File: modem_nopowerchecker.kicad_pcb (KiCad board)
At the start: 2 copper layers, 49.8 x 36.6 mm, 17 parts, among them P1 CONN_01X02, P2 CONN_01X02, P3 CONN_01X04, U1 PC817, U2 7805

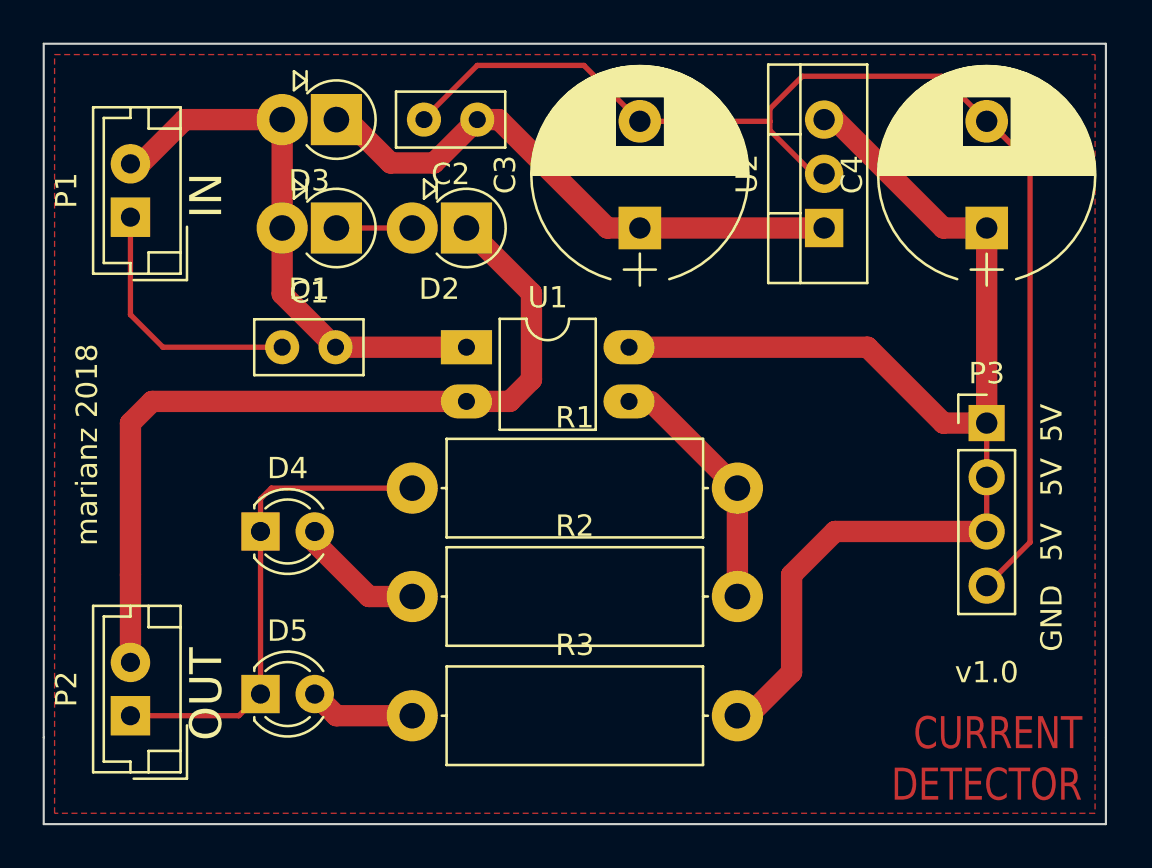
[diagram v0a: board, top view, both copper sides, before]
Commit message: +digital output pin
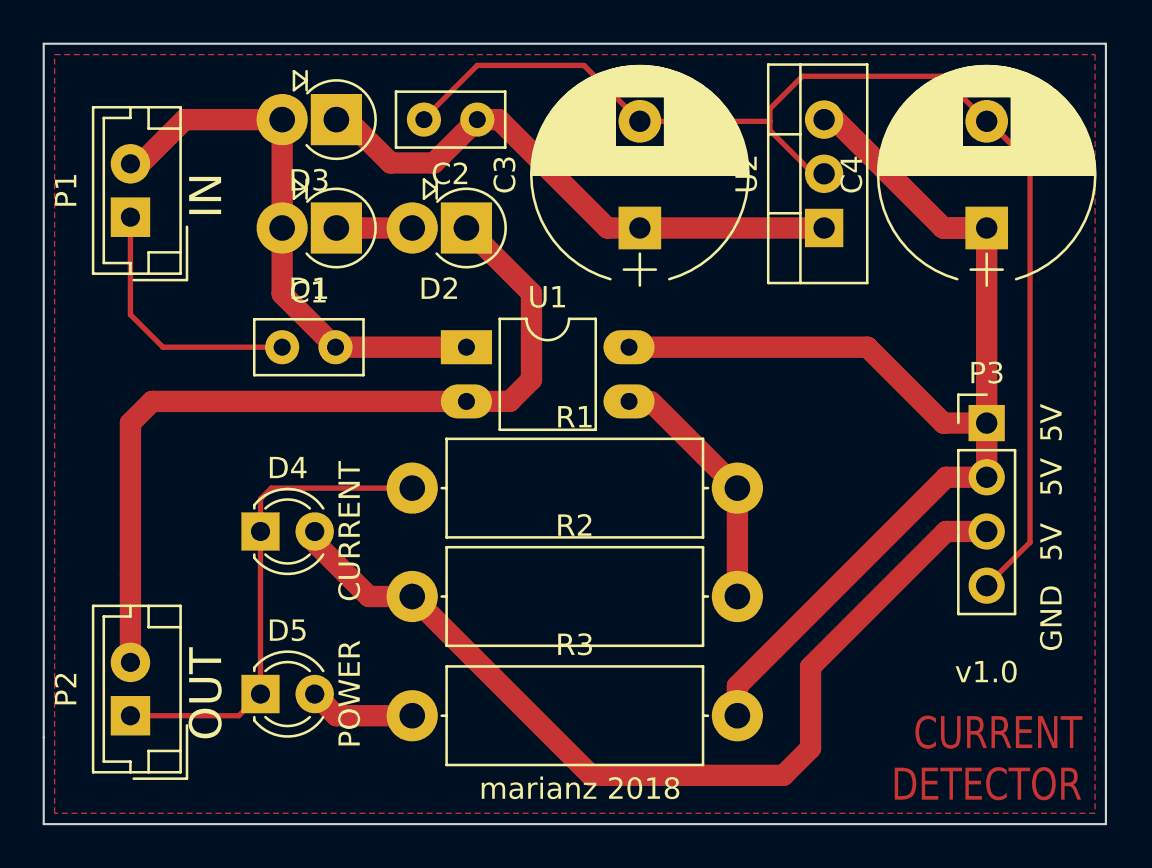
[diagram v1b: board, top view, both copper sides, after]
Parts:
- C1: value C -> 0.1uF
- C2: value C -> 0.1 uF
- C3, C4: value CP -> 100uF/16V
- D1, D2, D3: value D -> 1N4001
- R1, R2: value R -> 1K
- R3: value R -> 10K
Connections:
- P3 pad 3: +5V -> Net-(D4-Pad2)
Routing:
- net Net-(D4-Pad2): track 6.13 -> 43.5 mm
- net +5V: track 61.6 -> 68.0 mm
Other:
- board text added: "CURRENT"
- board text added: "POWER"
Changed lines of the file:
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@@
     (area 87.833999 81.229999 137.718001 117.906001)
     (thickness 1.6)
-    (drawings 15)
-    (tracks 75)
+    (drawings 17)
+    (tracks 81)
     (zones 0)
     (modules 17)
@@
       (outputformat 1)
       (mirror false)
-      (drillshape 1)
+      (drillshape 0)
       (scaleselection 1)
       (outputdirectory ""))
@@
       (effects (font (size 1 1) (thickness 0.15)))
     )
-    (fp_text value C (at 1.25 2.56) (layer F.Fab)
+    (fp_text value 0.1uF (at 1.25 2.56) (layer F.Fab)
       (effects (font (size 1 1) (thickness 0.15)))
     )
@@
       (effects (font (size 1 1) (thickness 0.15)))
     )
-    (fp_text value C (at 1.25 2.56 180) (layer F.Fab)
+    (fp_text value "0.1 uF" (at 1.524 2.286 180) (layer F.Fab)
       (effects (font (size 1 1) (thickness 0.15)))
     )
@@
       (effects (font (size 1 1) (thickness 0.15)))
     )
-    (fp_text value CP (at 2.5 6.31 90) (layer F.Fab)
+    (fp_text value 100uF/16V (at 2.5 6.31 90) (layer F.Fab)
       (effects (font (size 1 1) (thickness 0.15)))
     )
@@
       (effects (font (size 1 1) (thickness 0.15)))
     )
-    (fp_text value CP (at 2.5 6.31 90) (layer F.Fab)
+    (fp_text value 100uF/16V (at 2.5 6.31 90) (layer F.Fab)
       (effects (font (size 1 1) (thickness 0.15)))
     )
@@
       (effects (font (size 1 1) (thickness 0.15)))
     )
-    (fp_text value D (at 1.27 3.749 180) (layer F.Fab)
+    (fp_text value 1N4001 (at 1.27 3.749 180) (layer F.Fab)
       (effects (font (size 1 1) (thickness 0.15)))
     )
@@
       (effects (font (size 1 1) (thickness 0.15)))
     )
-    (fp_text value D (at 1.27 3.749 180) (layer F.Fab)
+    (fp_text value 1N4001 (at 1.27 3.749 180) (layer F.Fab)
       (effects (font (size 1 1) (thickness 0.15)))
     )
@@
       (effects (font (size 1 1) (thickness 0.15)))
     )
-    (fp_text value R (at 7.62 3.31) (layer F.Fab)
+    (fp_text value 1K (at 7.62 3.31) (layer F.Fab)
       (effects (font (size 1 1) (thickness 0.15)))
     )
@@
       (effects (font (size 1 1) (thickness 0.15)))
     )
-    (fp_text value R (at 7.62 3.31) (layer F.Fab)
+    (fp_text value 1K (at 7.62 3.31) (layer F.Fab)
       (effects (font (size 1 1) (thickness 0.15)))
     )
@@
       (effects (font (size 1 1) (thickness 0.15)))
     )
-    (fp_text value R (at 7.62 3.31) (layer F.Fab)
+    (fp_text value 10K (at 7.62 3.31) (layer F.Fab)
       (effects (font (size 1 1) (thickness 0.15)))
     )
@@
       (effects (font (size 1 1) (thickness 0.15)))
     )
-    (fp_text value D (at 1.27 3.749 180) (layer F.Fab)
+    (fp_text value 1N4001 (at 1.27 2.286 180) (layer F.Fab)
       (effects (font (size 1 1) (thickness 0.15)))
     )
@@
       (net 4 +5V))
     (pad 3 thru_hole oval (at 0 5.08) (size 1.7 1.7) (drill 1) (layers *.Cu *.Mask)
-      (net 4 +5V))
+      (net 7 "Net-(D4-Pad2)"))
     (pad 4 thru_hole oval (at 0 7.62) (size 1.7 1.7) (drill 1) (layers *.Cu *.Mask)
       (net 1 GND))
@@
     )
   )
-  (gr_text "marianz 2018" (at 89.916 100.076 90) (layer F.SilkS)
+  (gr_text CURRENT (at 102.235 104.14 90) (layer F.SilkS)
+    (effects (font (size 1 1) (thickness 0.2)))
+  )
+  (gr_text POWER (at 102.235 111.76 90) (layer F.SilkS)
+    (effects (font (size 1 1) (thickness 0.2)))
+  )
+  (gr_text "marianz 2018" (at 113.03 116.205) (layer F.SilkS)
     (effects (font (size 1 1) (thickness 0.1)))
   )
@@
   (segment (start 106.172 86.868) (end 108.204 84.836) (width 1) (layer F.Cu) (net 3))
   (segment (start 104.14 86.868) (end 106.172 86.868) (width 1) (layer F.Cu) (net 3))
-  (segment (start 132.08 104.14) (end 124.968 104.14) (width 1) (layer F.Cu) (net 4))
-  (segment (start 124.968 104.14) (end 122.936 106.172) (width 1) (layer F.Cu) (net 4))
-  (segment (start 122.936 106.172) (end 122.936 110.744) (width 1) (layer F.Cu) (net 4))
-  (segment (start 122.936 110.744) (end 120.904 112.776) (width 1) (layer F.Cu) (net 4))
-  (segment (start 120.904 112.776) (end 120.396 112.776) (width 0.25) (layer F.Cu) (net 4))
+  (segment (start 132.08 101.6) (end 130.175 101.6) (width 1) (layer F.Cu) (net 4))
+  (segment (start 120.396 111.379) (end 120.396 112.776) (width 1) (layer F.Cu) (net 4))
+  (segment (start 130.175 101.6) (end 120.396 111.379) (width 1) (layer F.Cu) (net 4))
+  (segment (start 132.08 89.916) (end 132.08 99.06) (width 1) (layer F.Cu) (net 4))
   (segment (start 115.316 95.504) (end 126.492 95.504) (width 1) (layer F.Cu) (net 4))
   (segment (start 126.492 95.504) (end 130.048 99.06) (width 1) (layer F.Cu) (net 4))
   (segment (start 130.048 99.06) (end 132.08 99.06) (width 1) (layer F.Cu) (net 4))
-  (segment (start 132.08 99.06) (end 132.08 101.6) (width 0.25) (layer F.Cu) (net 4))
-  (segment (start 132.08 101.6) (end 132.08 104.14) (width 0.25) (layer F.Cu) (net 4))
+  (segment (start 132.08 99.06) (end 132.08 101.6) (width 1) (layer F.Cu) (net 4))
+  (segment (start 124.46 84.836) (end 124.968 84.836) (width 1) (layer F.Cu) (net 4))
+  (segment (start 124.968 84.836) (end 130.048 89.916) (width 1) (layer F.Cu) (net 4))
+  (segment (start 130.048 89.916) (end 132.08 89.916) (width 1) (layer F.Cu) (net 4))
   (segment (start 120.904 112.776) (end 120.396 112.776) (width 0.25) (layer F.Cu) (net 4))
-  (segment (start 132.08 89.916) (end 132.08 99.06) (width 1) (layer F.Cu) (net 4))
-  (segment (start 124.46 84.836) (end 124.968 84.836) (width 0.25) (layer F.Cu) (net 4))
+  (segment (start 120.904 112.776) (end 120.396 112.776) (width 0.25) (layer F.Cu) (net 4))
   (segment (start 124.968 84.836) (end 130.048 89.916) (width 1) (layer F.Cu) (net 4))
   (segment (start 130.048 89.916) (end 132.08 89.916) (width 1) (layer F.Cu) (net 4))
   (segment (start 115.316 95.504) (end 116.332 95.504) (width 0.25) (layer F.Cu) (net 4))
-  (segment (start 101.6 89.916) (end 105.156 89.916) (width 0.25) (layer F.Cu) (net 5))
+  (segment (start 101.6 89.916) (end 105.156 89.916) (width 1) (layer F.Cu) (net 5))
   (segment (start 91.948 106.172) (end 91.948 110.276) (width 1) (layer F.Cu) (net 6))
   (segment (start 107.696 98.044) (end 92.964 98.044) (width 1) (layer F.Cu) (net 6))
@@
   (segment (start 110.744 97.028) (end 109.728 98.044) (width 1) (layer F.Cu) (net 6))
   (segment (start 109.728 98.044) (end 107.696 98.044) (width 1) (layer F.Cu) (net 6))
+  (segment (start 132.08 104.14) (end 130.175 104.14) (width 1) (layer F.Cu) (net 7))
+  (segment (start 113.538 115.57) (end 105.156 107.188) (width 1) (layer F.Cu) (net 7))
+  (segment (start 122.555 115.57) (end 113.538 115.57) (width 1) (layer F.Cu) (net 7))
+  (segment (start 123.825 114.3) (end 122.555 115.57) (width 1) (layer F.Cu) (net 7))
+  (segment (start 123.825 110.49) (end 123.825 114.3) (width 1) (layer F.Cu) (net 7))
+  (segment (start 130.175 104.14) (end 123.825 110.49) (width 1) (layer F.Cu) (net 7))
   (segment (start 100.584 104.14) (end 100.584 104.648) (width 0.25) (layer F.Cu) (net 7))
   (segment (start 100.584 104.648) (end 103.124 107.188) (width 1) (layer F.Cu) (net 7))

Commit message: *traces path
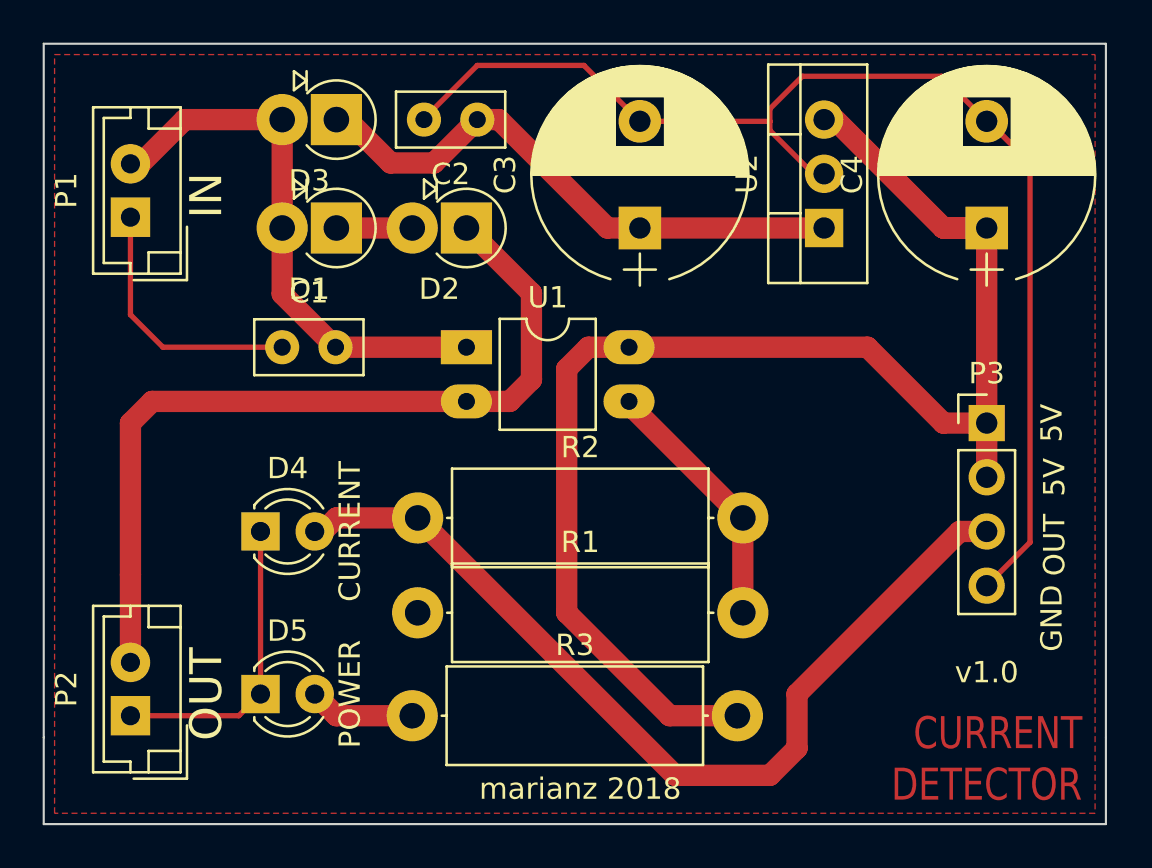
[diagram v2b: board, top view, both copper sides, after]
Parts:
- moved R1 5.85 mm to (105.4, 108.0)
- moved R2 3.69 mm to (105.4, 103.5)
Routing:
- net GND: track 96.0 -> 87.1 mm
- net +5V: track 68.0 -> 75.7 mm
- net Net-(R1-Pad2): track 11.8 -> 13.1 mm
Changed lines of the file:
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@@
     (thickness 1.6)
     (drawings 17)
-    (tracks 81)
+    (tracks 82)
     (zones 0)
     (modules 17)
@@
   )
   (module Resistors_ThroughHole:R_Axial_DIN0414_L11.9mm_D4.5mm_P15.24mm_Horizontal (layer F.Cu)
-    (at 105.156 102.108)
+    (at 105.41 107.95)
     (descr "Resistor, Axial_DIN0414 series, Axial, Horizontal, pin pitch=15.24mm, 2W, length*diameter=11.9*4.5mm^2, http://www.vishay.com/docs/20128/wkxwrx.pdf")
     (tags "Resistor Axial_DIN0414 series Axial Horizontal pin pitch 15.24mm 2W length 11.9mm diameter 4.5mm")
@@
   )
   (module Resistors_ThroughHole:R_Axial_DIN0414_L11.9mm_D4.5mm_P15.24mm_Horizontal (layer F.Cu)
-    (at 105.156 107.188)
+    (at 105.41 103.505)
     (descr "Resistor, Axial_DIN0414 series, Axial, Horizontal, pin pitch=15.24mm, 2W, length*diameter=11.9*4.5mm^2, http://www.vishay.com/docs/20128/wkxwrx.pdf")
     (tags "Resistor Axial_DIN0414 series Axial Horizontal pin pitch 15.24mm 2W length 11.9mm diameter 4.5mm")
@@
     (effects (font (size 1 1) (thickness 0.2)))
   )
-  (gr_text 5V (at 135.128 101.6 90) (layer F.SilkS)
+  (gr_text 5V (at 135.255 101.6 90) (layer F.SilkS)
     (effects (font (size 1 1) (thickness 0.2)))
   )
-  (gr_text 5V (at 135.128 104.648 90) (layer F.SilkS)
+  (gr_text OUT (at 135.255 104.775 90) (layer F.SilkS)
     (effects (font (size 1 1) (thickness 0.2)))
   )
@@
   (segment (start 121.92 84.328) (end 123.444 82.804) (width 0.25) (layer F.Cu) (net 1))
   (segment (start 98.044 104.14) (end 98.044 111.76) (width 0.25) (layer F.Cu) (net 1))
-  (segment (start 105.156 102.108) (end 98.552 102.108) (width 0.25) (layer F.Cu) (net 1))
-  (segment (start 98.044 102.616) (end 98.044 104.14) (width 0.25) (layer F.Cu) (net 1))
-  (segment (start 98.552 102.108) (end 98.044 102.616) (width 0.25) (layer F.Cu) (net 1))
   (segment (start 115.824 84.916) (end 121.92 84.916) (width 0.25) (layer F.Cu) (net 1))
   (segment (start 124.46 87.376) (end 123.952 87.376) (width 0.25) (layer F.Cu) (net 1))
@@
   (segment (start 106.172 86.868) (end 108.204 84.836) (width 1) (layer F.Cu) (net 3))
   (segment (start 104.14 86.868) (end 106.172 86.868) (width 1) (layer F.Cu) (net 3))
-  (segment (start 132.08 101.6) (end 130.175 101.6) (width 1) (layer F.Cu) (net 4))
-  (segment (start 120.396 111.379) (end 120.396 112.776) (width 1) (layer F.Cu) (net 4))
-  (segment (start 130.175 101.6) (end 120.396 111.379) (width 1) (layer F.Cu) (net 4))
+  (segment (start 115.316 95.504) (end 113.411 95.504) (width 1) (layer F.Cu) (net 4))
+  (segment (start 117.221 112.776) (end 120.396 112.776) (width 1) (layer F.Cu) (net 4))
+  (segment (start 112.395 107.95) (end 117.221 112.776) (width 1) (layer F.Cu) (net 4))
+  (segment (start 112.395 96.52) (end 112.395 107.95) (width 1) (layer F.Cu) (net 4))
+  (segment (start 113.411 95.504) (end 112.395 96.52) (width 1) (layer F.Cu) (net 4))
   (segment (start 132.08 89.916) (end 132.08 99.06) (width 1) (layer F.Cu) (net 4))
   (segment (start 115.316 95.504) (end 126.492 95.504) (width 1) (layer F.Cu) (net 4))
@@
   (segment (start 110.744 97.028) (end 109.728 98.044) (width 1) (layer F.Cu) (net 6))
   (segment (start 109.728 98.044) (end 107.696 98.044) (width 1) (layer F.Cu) (net 6))
-  (segment (start 132.08 104.14) (end 130.175 104.14) (width 1) (layer F.Cu) (net 7))
-  (segment (start 113.538 115.57) (end 105.156 107.188) (width 1) (layer F.Cu) (net 7))
-  (segment (start 122.555 115.57) (end 113.538 115.57) (width 1) (layer F.Cu) (net 7))
-  (segment (start 123.825 114.3) (end 122.555 115.57) (width 1) (layer F.Cu) (net 7))
-  (segment (start 123.825 110.49) (end 123.825 114.3) (width 1) (layer F.Cu) (net 7))
-  (segment (start 130.175 104.14) (end 123.825 110.49) (width 1) (layer F.Cu) (net 7))
+  (segment (start 105.41 103.505) (end 101.6 103.505) (width 1) (layer F.Cu) (net 7))
+  (segment (start 101.6 103.505) (end 100.965 104.14) (width 1) (layer F.Cu) (net 7))
+  (segment (start 100.965 104.14) (end 100.584 104.14) (width 1) (layer F.Cu) (net 7))
+  (segment (start 132.08 104.14) (end 130.81 104.14) (width 1) (layer F.Cu) (net 7))
+  (segment (start 117.475 115.57) (end 105.41 103.505) (width 1) (layer F.Cu) (net 7))
+  (segment (start 121.92 115.57) (end 117.475 115.57) (width 1) (layer F.Cu) (net 7))
+  (segment (start 123.19 114.3) (end 121.92 115.57) (width 1) (layer F.Cu) (net 7))
+  (segment (start 123.19 111.76) (end 123.19 114.3) (width 1) (layer F.Cu) (net 7))
+  (segment (start 130.81 104.14) (end 123.19 111.76) (width 1) (layer F.Cu) (net 7))
   (segment (start 100.584 104.14) (end 100.584 104.648) (width 0.25) (layer F.Cu) (net 7))
-  (segment (start 100.584 104.648) (end 103.124 107.188) (width 1) (layer F.Cu) (net 7))
-  (segment (start 103.124 107.188) (end 105.156 107.188) (width 1) (layer F.Cu) (net 7))
   (segment (start 100.584 111.76) (end 101.6 112.776) (width 1) (layer F.Cu) (net 8))
   (segment (start 101.6 112.776) (end 105.156 112.776) (width 1) (layer F.Cu) (net 8))
-  (segment (start 120.396 102.108) (end 120.396 107.188) (width 1) (layer F.Cu) (net 9))
+  (segment (start 120.65 103.505) (end 120.65 107.95) (width 1) (layer F.Cu) (net 9))
+  (segment (start 115.316 98.044) (end 115.316 98.171) (width 1) (layer F.Cu) (net 9))
+  (segment (start 115.316 98.171) (end 120.65 103.505) (width 1) (layer F.Cu) (net 9))
   (segment (start 115.316 98.044) (end 116.332 98.044) (width 0.25) (layer F.Cu) (net 9))
-  (segment (start 116.332 98.044) (end 120.396 102.108) (width 1) (layer F.Cu) (net 9))
   (zone (net 1) (net_name GND) (layer F.Cu) (hatch edge 0.508)
     (connect_pads (clearance 0.508))
